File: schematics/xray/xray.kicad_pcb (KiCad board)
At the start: 4 copper layers, 130 x 65 mm, 103 parts, among them J1 USB_A, J2 USB_B_Micro, J3 USB_C_Receptacle_USB2.0, J4 USBASP, M1 VibroMotor, 3V, 8x2.7mm, Q1 IRF7413ZPbF, Q10 IRLML0030, Q11 IRLML0030, Q2 IRF7424PBF, Q3 IRLML0030, Q4 IRF7424PBF, Q5 IRLML0030, Q6 BC857, Q7 BC847, Q8 IRLML0030, Q9 IRLML0030, SW1 EC11W****, T1 Transformer_1P_1S, U1 IP5328P, U2 ATmega328P-A, U3 SN74LVC2T45DCUR, U4 SN74LVC2T45DCUR, U5 SN74LVC2T45DCUR, U6 Display_1.18inch_st7535, Y1 HC-49SM, 8MHz

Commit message: debugging...
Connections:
- U2 pad 13: SPEAKER -> USB_INT
- U2 pad 14: FLASHLIGHT -> SPEAKER
- U2 pad 9: USB_INT -> FLASHLIGHT
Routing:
- net FLASHLIGHT: track 61.8 -> 59.3 mm
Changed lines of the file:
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@@
       (net 37 "Net-(C31-Pad1)") (pinfunction "XTAL2/PB7") (pintype "bidirectional"))
     (pad "9" smd rect (at -2.8 4.25 90) (size 1.6 0.55) (layers "F.Cu" "F.Paste" "F.Mask")
-      (net 39 "USB_INT") (pinfunction "PD5") (pintype "bidirectional"))
+      (net 35 "FLASHLIGHT") (pinfunction "PD5") (pintype "bidirectional"))
     (pad "10" smd rect (at -2 4.25 90) (size 1.6 0.55) (layers "F.Cu" "F.Paste" "F.Mask")
       (net 38 "VIBRO") (pinfunction "PD6") (pintype "bidirectional"))
@@
       (net 45 "ENCODER_CLICK") (pinfunction "PB0") (pintype "bidirectional"))
     (pad "13" smd rect (at 0.4 4.25 90) (size 1.6 0.55) (layers "F.Cu" "F.Paste" "F.Mask")
-      (net 15 "SPEAKER") (pinfunction "PB1") (pintype "bidirectional"))
+      (net 39 "USB_INT") (pinfunction "PB1") (pintype "bidirectional"))
     (pad "14" smd rect (at 1.2 4.25 90) (size 1.6 0.55) (layers "F.Cu" "F.Paste" "F.Mask")
-      (net 35 "FLASHLIGHT") (pinfunction "PB2") (pintype "bidirectional"))
+      (net 15 "SPEAKER") (pinfunction "PB2") (pintype "bidirectional"))
     (pad "15" smd rect (at 2 4.25 90) (size 1.6 0.55) (layers "F.Cu" "F.Paste" "F.Mask")
       (net 59 "MOSI") (pinfunction "PB3") (pintype "bidirectional"))
@@
   (segment (start 78.01 101.54) (end 78.26 101.29) (width 1) (layer "F.Cu") (net 14))
   (segment (start 97.0475 101.04) (end 96.01 102.0775) (width 1) (layer "F.Cu") (net 14))
-  (segment (start 148.41 129.44) (end 149.26 130.29) (width 0.3) (layer "F.Cu") (net 15))
-  (segment (start 149.26 130.29) (end 149.26 132.79) (width 0.3) (layer "F.Cu") (net 15))
+  (segment (start 149.21 132.84) (end 149.21 127.79) (width 0.25) (layer "F.Cu") (net 15))
   (segment (start 148.0975 133.9525) (end 145.76 133.9525) (width 0.3) (layer "F.Cu") (net 15))
-  (segment (start 149.26 132.79) (end 148.0975 133.9525) (width 0.3) (layer "F.Cu") (net 15))
+  (segment (start 148.0975 133.9525) (end 149.21 132.84) (width 0.25) (layer "F.Cu") (net 15))
   (segment (start 145.7225 133.99) (end 145.76 133.9525) (width 0.3) (layer "F.Cu") (net 15))
   (segment (start 143.1975 133.99) (end 145.7225 133.99) (width 0.3) (layer "F.Cu") (net 15))
-  (segment (start 148.41 127.79) (end 148.41 129.44) (width 0.3) (layer "F.Cu") (net 15))
   (segment (start 175.055 109.065) (end 178.105 112.115) (width 1) (layer "F.Cu") (net 16))
   (segment (start 170.01 110.765) (end 170.035 110.74) (width 1) (layer "F.Cu") (net 16))
@@
   (segment (start 145.21 117.74) (end 145.21 119.29) (width 0.3) (layer "F.Cu") (net 34))
   (segment (start 103.51 112.1025) (end 101.01 114.6025) (width 0.5) (layer "F.Cu") (net 34))
-  (segment (start 149.21 125.8304) (end 149.21 127.79) (width 0.3) (layer "F.Cu") (net 35))
-  (via (at 149.21 125.8304) (size 0.6) (drill 0.4) (layers "F.Cu" "B.Cu") (net 35))
+  (segment (start 145.21 125.84) (end 145.21 127.79) (width 0.25) (layer "F.Cu") (net 35))
+  (segment (start 146.26 124.79) (end 145.21 125.84) (width 0.25) (layer "F.Cu") (net 35))
+  (via (at 146.26 124.79) (size 0.6) (drill 0.4) (layers "F.Cu" "B.Cu") (net 35))
   (via (at 110.96 120.09) (size 0.6) (drill 0.4) (layers "F.Cu" "B.Cu") (net 35))
-  (segment (start 124.01 124.04) (end 148.51 124.04) (width 0.3) (layer "In1.Cu") (net 35))
-  (segment (start 108.052894 128.79) (end 119.26 128.79) (width 0.3) (layer "In1.Cu") (net 35))
-  (segment (start 110.96 120.09) (end 107.01 124.04) (width 0.3) (layer "In1.Cu") (net 35))
-  (segment (start 107.01 124.04) (end 107.01 127.747106) (width 0.3) (layer "In1.Cu") (net 35))
-  (segment (start 119.26 128.79) (end 124.01 124.04) (width 0.3) (layer "In1.Cu") (net 35))
-  (segment (start 148.51 124.04) (end 149.21 124.74) (width 0.3) (layer "In1.Cu") (net 35))
-  (segment (start 107.01 127.747106) (end 108.052894 128.79) (width 0.3) (layer "In1.Cu") (net 35))
-  (segment (start 149.21 124.74) (end 149.21 125.8304) (width 0.3) (layer "In1.Cu") (net 35))
+  (segment (start 146.26 124.79) (end 145.51 124.04) (width 0.3) (layer "In1.Cu") (net 35))
+  (segment (start 124.01 124.04) (end 119.26 128.79) (width 0.3) (layer "In1.Cu") (net 35))
+  (segment (start 119.26 128.79) (end 108.052894 128.79) (width 0.3) (layer "In1.Cu") (net 35))
+  (segment (start 145.51 124.04) (end 124.01 124.04) (width 0.3) (layer "In1.Cu") (net 35))
+  (segment (start 108.052894 128.79) (end 107.01 127.747106) (width 0.3) (layer "In1.Cu") (net 35))
+  (segment (start 107.01 124.04) (end 110.96 120.09) (width 0.3) (layer "In1.Cu") (net 35))
+  (segment (start 107.01 127.747106) (end 107.01 124.04) (width 0.3) (layer "In1.Cu") (net 35))
   (segment (start 108.9475 120.09) (end 110.96 120.09) (width 0.3) (layer "B.Cu") (net 35))
   (segment (start 113.4725 120.09) (end 113.51 120.1275) (width 0.3) (layer "B.Cu") (net 35))
@@
   (segment (start 143.6725 138.4525) (end 142.26 137.04) (width 0.3) (layer "B.Cu") (net 38))
   (segment (start 142.01 131.04) (end 143.01 130.04) (width 0.3) (layer "B.Cu") (net 38))
+  (segment (start 149.76 125.04) (end 148.41 126.39) (width 0.25) (layer "F.Cu") (net 39))
+  (segment (start 148.41 126.39) (end 148.41 127.79) (width 0.25) (layer "F.Cu") (net 39))
+  (segment (start 149.76 124.54) (end 149.76 125.04) (width 0.25) (layer "F.Cu") (net 39))
   (segment (start 166.009999 101.79) (end 167.06 101.79) (width 0.2) (layer "F.Cu") (net 39))
   (segment (start 165.858175 101.638176) (end 166.009999 101.79) (width 0.2) (layer "F.Cu") (net 39))
-  (segment (start 145.21 126.259239) (end 145.21 127.79) (width 0.3) (layer "F.Cu") (net 39))
-  (segment (start 146.429239 125.04) (end 145.21 126.259239) (width 0.3) (layer "F.Cu") (net 39))
-  (via (at 146.429239 125.04) (size 0.6) (drill 0.4) (layers "F.Cu" "B.Cu") (net 39))
+  (via (at 149.76 124.54) (size 0.6) (drill 0.4) (layers "F.Cu" "B.Cu") (net 39))
   (via (at 165.858175 101.638176) (size 0.6) (drill 0.4) (layers "F.Cu" "B.Cu") (net 39))
+  (segment (start 152.16 122.14) (end 154.258529 122.14) (width 0.3) (layer "In2.Cu") (net 39))
+  (segment (start 149.76 124.54) (end 152.16 122.14) (width 0.3) (layer "In2.Cu") (net 39))
+  (segment (start 154.61 121.788529) (end 154.61 116.859239) (width 0.3) (layer "In2.Cu") (net 39))
   (segment (start 165.01 102.486351) (end 165.858175 101.638176) (width 0.3) (layer "In2.Cu") (net 39))
-  (segment (start 146.429239 125.04) (end 165.01 106.459239) (width 0.3) (layer "In2.Cu") (net 39))
+  (segment (start 154.61 116.859239) (end 165.01 106.459239) (width 0.3) (layer "In2.Cu") (net 39))
+  (segment (start 154.258529 122.14) (end 154.61 121.788529) (width 0.3) (layer "In2.Cu") (net 39))
   (segment (start 165.01 106.459239) (end 165.01 102.486351) (width 0.3) (layer "In2.Cu") (net 39))
   (segment (start 100.0975 120.04) (end 99.5475 120.59) (width 0.5) (layer "F.Cu") (net 40))
@@
   (segment (start 114.4 111.79) (end 116.985 111.79) (width 1) (layer "B.Cu") (net 44))
   (segment (start 113.15 110.54) (end 114.4 111.79) (width 1) (layer "B.Cu") (net 44))
-  (segment (start 148.01 125.79) (end 147.61 126.19) (width 0.3) (layer "F.Cu") (net 45))
-  (segment (start 147.61 126.19) (end 147.61 127.79) (width 0.3) (layer "F.Cu") (net 45))
-  (via (at 148.01 125.79) (size 0.6) (drill 0.4) (layers "F.Cu" "B.Cu") (net 45))
-  (segment (start 148.01 125.79) (end 148.01 124.79) (width 0.3) (layer "B.Cu") (net 45))
-  (segment (start 144.26 121.04) (end 139.564213 121.04) (width 0.3) (layer "B.Cu") (net 45))
+  (segment (start 148.094266 125.374266) (end 147.61 125.858532) (width 0.3) (layer "F.Cu") (net 45))
+  (segment (start 147.61 125.858532) (end 147.61 127.79) (width 0.3) (layer "F.Cu") (net 45))
+  (via (at 148.094266 125.374266) (size 0.6) (drill 0.4) (layers "F.Cu" "B.Cu") (net 45))
   (segment (start 124.51 108.815) (end 126.235 110.54) (width 1) (layer "B.Cu") (net 45))
-  (segment (start 148.01 124.79) (end 144.26 121.04) (width 0.3) (layer "B.Cu") (net 45))
-  (segment (start 126.235 110.54) (end 127.65 110.54) (width 1) (layer "B.Cu") (net 45))
   (segment (start 139.564213 121.04) (end 129.064213 110.54) (width 0.3) (layer "B.Cu") (net 45))
+  (segment (start 148.094266 125.374266) (end 148.094266 124.874266) (width 0.3) (layer "B.Cu") (net 45))
+  (segment (start 144.26 121.04) (end 139.564213 121.04) (width 0.3) (layer "B.Cu") (net 45))
+  (segment (start 126.235 110.54) (end 127.65 110.54) (width 1) (layer "B.Cu") (net 45))
   (segment (start 129.064213 110.54) (end 127.65 110.54) (width 0.3) (layer "B.Cu") (net 45))
+  (segment (start 148.094266 124.874266) (end 144.26 121.04) (width 0.3) (layer "B.Cu") (net 45))
   (segment (start 107.41 110.24) (end 107.51 110.34) (width 1) (layer "B.Cu") (net 46))
   (segment (start 58.51 110.24) (end 58.51 105.84) (width 1) (layer "B.Cu") (net 46))

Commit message: continue working under firmware and schematics
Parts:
- added C39: 100 nF, Capacitor_SMD:C_0603_1608Metric, F.Cu at (147.8, 130.8)
- added C7: 200 pF, Capacitor_SMD:C_1206_3216Metric, B.Cu at (140.3, 114.5)
- added R23: 1M, Resistor_SMD:R_0805_2012Metric, B.Cu at (161.0, 130.0)
- added R25: RSET [?], Resistor_SMD:R_0805_2012Metric, B.Cu at (152.0, 124.5)
- added R7: 200K, Resistor_SMD:R_0805_2012Metric, B.Cu at (153.5, 118.5)
- added SW2: B3F3150, Button_Switch_THT:SW_Tactile_SKHH_Angled, F.Cu at (101.0, 137.4)
- added U1: PCA9306, Package_SO:MSOP-8_3x3mm_P0.65mm, B.Cu at (143.8, 114.5)
- BT1: value Li-Ion, 3.7V, 10000 mAh, 1260100 -> Li-Ion, 4.2V, 10000 mAh, 1260100
- moved R27 6.39 mm to (100.5, 129.8)
- moved Q9 6.11 mm to (96.8, 130.0)
- moved C38 5.00 mm to (156.0, 135.0)
- renumbered C7 to C10, C14 to C11, C8 to C12, C9 to C13, C18 to C14, C11 to C15, C12 to C16, C15 to C18, C16 to C19, C24 to C20, C19 to C21, C20 to C22, C21 to C23, C23 to C24, C22 to C25, C25 to C26, C26 to C27, C29 to C28, C27 to C29, C33 to C32, C28 to C33, C32 to C34, C34 to C35, C35 to C36, C36 to C37, C37 to C38, C10 to C8, C13 to C9, Q6 to Q5, Q5 to Q6, R5 to R10, R6 to R11, R9 to R12, R10 to R13, R12 to R14, R16 to R15, R11 to R16, R13 to R17, R20 to R2, R14 to R20, R15 to R21, R17 to R22, R22 to R24, R23 to R26, R24 to R27, R25 to R28, R26 to R29, R21 to R3, R27 to R30, R2 to R4, R3 to R5, R4 to R6, R7 to R8, R8 to R9, U1 to U2, U2 to U3, U3 to U4, U4 to U5, U5 to U6, U6 to U7
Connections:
- R2 pad 2: I2C_SCL -> USB_I2C_SCL
- R3 pad 2: I2C_SDA -> USB_I2C_SDA
- U2 pad 11: I2C_SCL -> USB_I2C_SCL
- U2 pad 12: I2C_SDA -> USB_I2C_SDA
- U3 pad 11: USB_FORCE_ON -> WAKEUP_BUTTON
- U3 pad 19: unconnected-(U2-Pad19) -> USB_FORCE_ON
- U3 pad 22: unconnected-(U2-Pad22) -> USB_I2C_ENABLE
- U3 pad 27: I2C_SDA -> MCU_I2C_SDA
- U3 pad 28: I2C_SCL -> MCU_I2C_SCL
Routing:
- net GND: track 589.0 -> 652.3 mm
- net WAKEUP_BUTTON: track 0.00 -> 52.7 mm, vias 0 -> 1
- net USB_I2C_SCL: track 0.00 -> 44.6 mm, vias 0 -> 2
- net USB_I2C_SDA: track 0.00 -> 44.5 mm, vias 0 -> 2
- net I2C_SCL: track 41.3 -> 0.00 mm, vias 2 -> 0
- net I2C_SDA: track 41.0 -> 0.00 mm, vias 2 -> 0
- net VREG: track 57.8 -> 89.0 mm, vias 3 -> 4
- net Net-(C7-Pad2): track 0.00 -> 17.4 mm
- net MCU_I2C_SCL: track 0.00 -> 9.22 mm, vias 0 -> 1
- net TFT_RESET: track 104.0 -> 97.1 mm
- net MCU_I2C_SDA: track 0.00 -> 6.42 mm, vias 0 -> 1
- net USB_I2C_ENABLE: track 0.00 -> 5.76 mm, vias 0 -> 1
- net VCC: track 443.9 -> 438.8 mm, vias 10 -> 9
- net Net-(C38-Pad1): track 11.5 -> 6.53 mm
- net TFT_DC: track 97.4 -> 92.9 mm
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
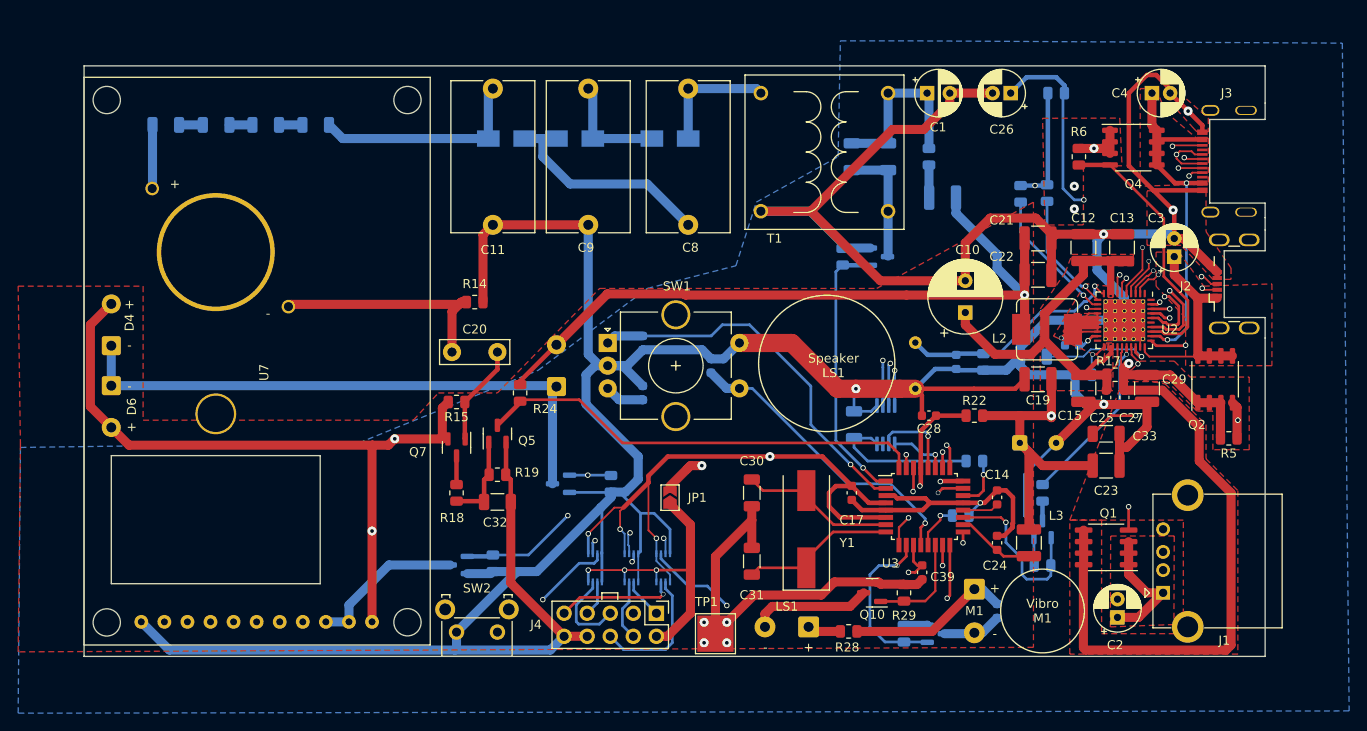
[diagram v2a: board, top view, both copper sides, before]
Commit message: fixed display schematics
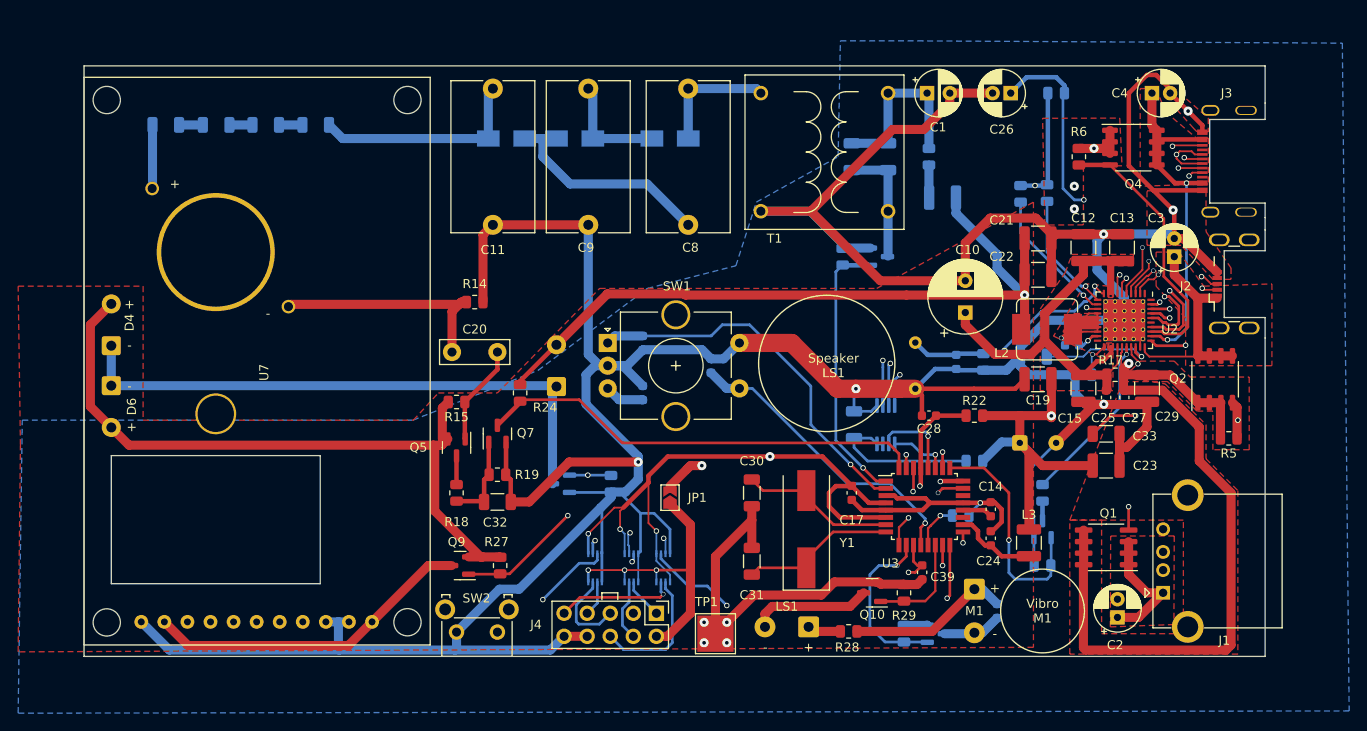
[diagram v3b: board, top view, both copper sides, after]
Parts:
- Q9: value IRLML0030 -> IRLML5203; moved to F.Cu
- R27: moved to F.Cu
- moved C14 1.48 mm to (155.3, 123.8)
- moved C24 0.86 mm to (155.3, 127.0)
- moved R27 0.84 mm to (101.3, 130.0)
- moved Q9 0.16 mm to (96.9, 130.0)
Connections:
- Q9 pad 1: TFT_ENABLE -> TFT_ENABLE#
- Q9 pad 2: GND -> VCC
- Q9 pad 3: Net-(Q9-Pad3) -> Net-(U7-Pad11)
- R27 pad 1: GND -> TFT_ENABLE#
- R27 pad 2: TFT_ENABLE -> VCC
- R7 pad 1: USB_I2C_ENABLE -> VCC
- U3 pad 19: USB_FORCE_ON -> unconnected-(U3-Pad19)
- U3 pad 22: USB_I2C_ENABLE -> unconnected-(U3-Pad22)
- U3 pad 24: TFT_ENABLE -> TFT_ENABLE#
- U3 pad 25: TFT_RESET -> USB_FORCE_ON
- U7 pad 10: Net-(Q9-Pad3) -> GND
- U7 pad 11: VCC -> Net-(U7-Pad11)
- U7 pad 2: TFT_RESET -> Net-(U7-Pad11)
- U7 pad 9: Net-(Q9-Pad3) -> GND
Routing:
- net TFT_RESET: track 97.1 -> 0.00 mm, vias 1 -> 0
- net TFT_ENABLE#: track 0.00 -> 58.8 mm, vias 0 -> 2
- net TFT_ENABLE: track 58.1 -> 0.00 mm, vias 2 -> 0
- net Net-(U7-Pad11): track 0.00 -> 36.3 mm
- net VCC: track 438.8 -> 404.1 mm, vias 9 -> 7
- net Net-(Q9-Pad3): track 17.4 -> 0.00 mm
- net USB_FORCE_ON: track 19.1 -> 25.7 mm
- net GND: track 652.3 -> 646.2 mm, vias 10 -> 11
- net USB_I2C_ENABLE: track 5.76 -> 0.00 mm, vias 1 -> 0
- net Net-(C14-Pad1): track 4.01 -> 3.33 mm

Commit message: continue working under schematics and firmware
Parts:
- added C40: 100 uF, Capacitor_THT:CP_Radial_D5.0mm_P2.50mm, F.Cu at (107.7, 129.8)
- added Q11: IRLML0030, Package_TO_SOT_SMD:SOT-23, B.Cu at (100.9, 130.2)
- added Q14: IRLML0030, Package_TO_SOT_SMD:SOT-23, B.Cu at (105.7, 125.0)
- added Q9: IRLML5203, Package_TO_SOT_SMD:SOT-23, B.Cu at (96.5, 127.4)
- added R27: 10K, Resistor_SMD:R_0805_2012Metric, B.Cu at (96.5, 131.4)
- added R28: 200K, Resistor_SMD:R_0805_2012Metric, B.Cu at (97.4, 124.0)
- added R32: 200K, Resistor_SMD:R_0805_2012Metric, B.Cu at (101.1, 126.0)
- R23, R26, R4: value 1M -> 200K
- R29: renamed from R27; value 1M -> 200K
- R31: renamed from R29; value 1M -> 200K
- R33: renamed from R30; value 1M -> 200K
- moved R22 0.10 mm to (153.5, 113.6)
- renumbered C39 to C38, C38 to C39, Q9 to Q10, Q10 to Q12, Q11 to Q13, R28 to R30
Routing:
- net Net-(C40-Pad1): track 0.00 -> 15.6 mm
- net WAKEUP_BUTTON: track 52.7 -> 65.1 mm
- net VCC: track 404.1 -> 412.7 mm, vias 7 -> 8
- net RESET: track 51.6 -> 57.7 mm, vias 2 -> 3
- net GND: track 646.2 -> 641.8 mm
- net Net-(R28-Pad1): track 0.00 -> 2.78 mm
- net Net-(Q9-Pad3): track 0.00 -> 2.47 mm

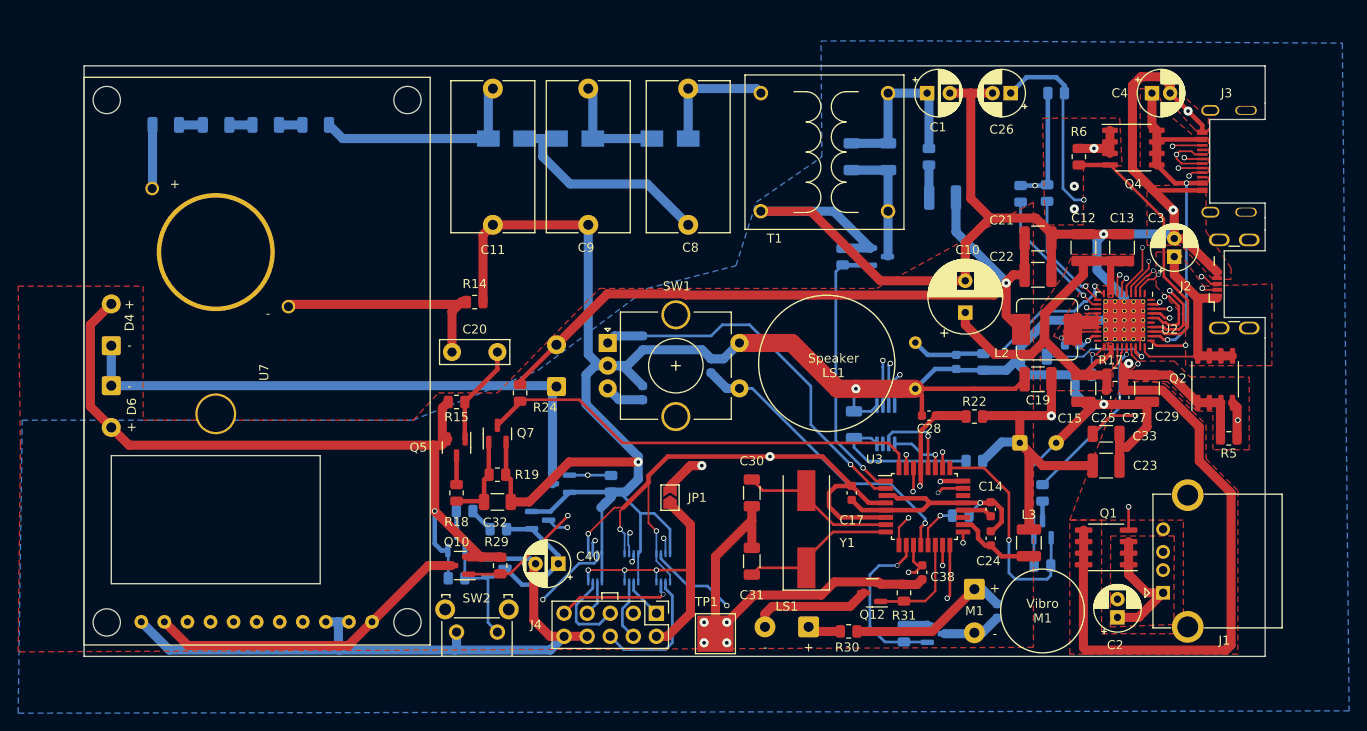
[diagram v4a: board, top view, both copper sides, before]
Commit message: added fuse to vbat
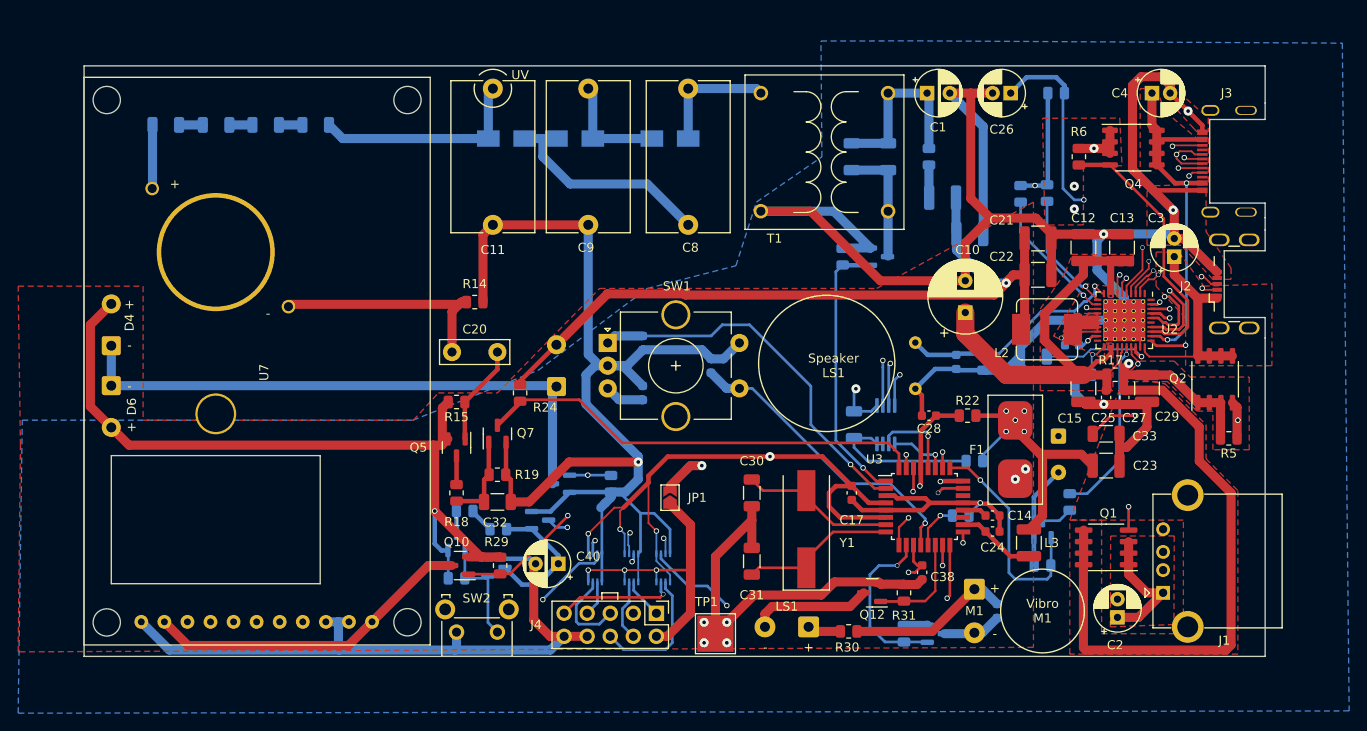
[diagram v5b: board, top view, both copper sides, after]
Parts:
- added F1: 1808, 6.3A, Library:FuseHolder1808, F.Cu at (158.0, 117.3)
- C19: moved to B.Cu
- moved C19 17.7 mm to (153.0, 93.5), turned to 0 degrees
- moved BT1 4.32 mm to (162.8, 115.8), turned to -90 degrees
- moved R20 3.16 mm to (164.0, 123.0)
- moved C24 0.78 mm to (155.5, 126.3), turned to 0 degrees
- moved R22 0.76 mm to (152.8, 113.5)
- moved C14 0.73 mm to (155.5, 124.5), turned to 0 degrees
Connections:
- BT1 pad 1: VCC -> Net-(BT1-Pad1)
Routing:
- net VCC: track 412.7 -> 387.5 mm, vias 8 -> 12
- net GND: track 641.8 -> 632.8 mm
- net Net-(BT1-Pad1): track 0.00 -> 6.72 mm, vias 0 -> 2
- net USB_VSYS: track 58.1 -> 63.3 mm
- net Net-(Q6-Pad3): track 2.15 -> 3.48 mm
- net USB_FORCE_ON: track 25.7 -> 24.7 mm
- net USB_KEY: track 19.0 -> 19.8 mm
- net RESET: track 57.7 -> 56.9 mm
- net Net-(C14-Pad1): track 3.33 -> 2.72 mm
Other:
- board text added: "UV"
